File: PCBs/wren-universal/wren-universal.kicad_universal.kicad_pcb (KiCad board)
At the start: 2 copper layers, 227.7 x 112.8 mm, 117 parts, among them J1 TRRS_Jack, SW0 Reset, U1 Elite-C

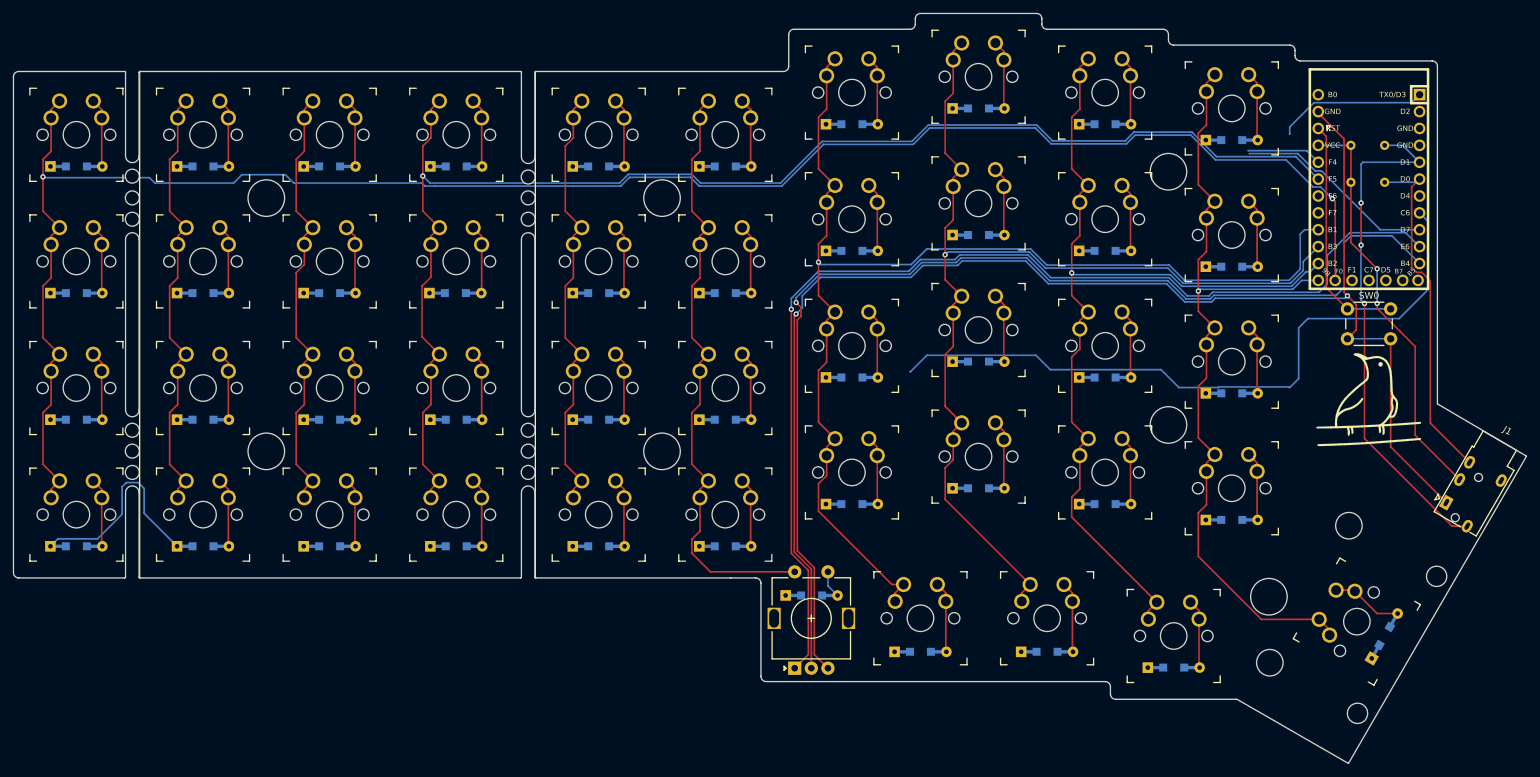
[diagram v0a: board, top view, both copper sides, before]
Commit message: Finish universal PCB and prepare for merge
Finished up the universal PCB (with breakoff tabs) and moved old individual PCBs to the legacy folder
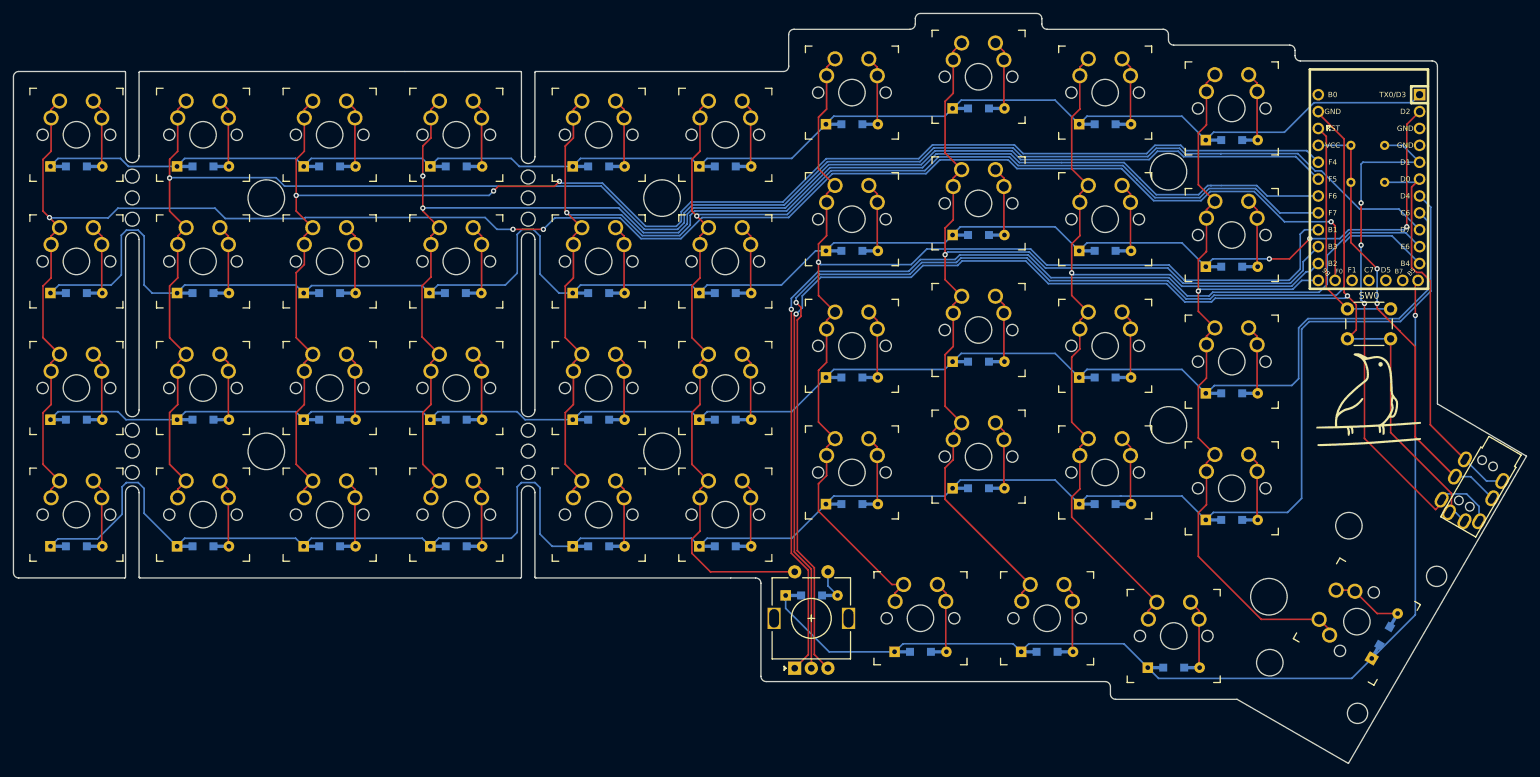
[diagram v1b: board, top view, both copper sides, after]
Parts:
- J1: footprint Connector_Audio:Jack_3.5mm_PJ320E_Horizontal -> footprints:TRRS_JACK_MJ4PP9
- moved J1 2.77 mm to (250.4, 93.0)
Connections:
- U1 pad 24: Net-(U1-Pad24) -> (no net)
- U1 pad 25: Net-(U1-Pad25) -> (no net)
- U1 pad 26: Net-(U1-Pad26) -> (no net)
- U1 pad 27: Net-(U1-Pad27) -> (no net)
- U1 pad 28: Net-(U1-Pad28) -> (no net)
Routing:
- net ROW1: track 0.00 -> 265.8 mm, vias 0 -> 3
- net ROW3: track 31.6 -> 291.3 mm
- net ROW0: track 22.6 -> 221.7 mm
- net COL8: track 96.7 -> 269.8 mm, vias 0 -> 1
- net ROW4: track 0.00 -> 157.6 mm, vias 0 -> 1
- net COL7: track 77.7 -> 231.9 mm, vias 0 -> 3
- net ROW2: track 103.7 -> 243.0 mm
- net COL5: track 66.5 -> 190.7 mm, vias 0 -> 1
- net COL4: track 92.5 -> 194.4 mm, vias 0 -> 1
- net VCC: track 62.0 -> 68.2 mm
- net SCL: track 52.6 -> 58.9 mm
- net SDA: track 77.7 -> 82.7 mm
- net GND: track 217.6 -> 222.4 mm
- net COL9: track 284.7 -> 282.3 mm, vias 2 -> 4
- net COL6: track 211.2 -> 211.9 mm, vias 1 -> 2
